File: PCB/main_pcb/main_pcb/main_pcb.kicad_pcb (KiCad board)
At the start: 2 copper layers, 235 x 235 mm, 49 parts, among them J1 Conn_01x20_Socket, J10 B6B-XH-A, J11 B8B-XH-A, J12 B6B-XH-A, J13 B8B-XH-A, J14 B8B-XH-A, J2 Conn_01x20_Socket, J3 B02P-VL, J4 B02P-VL, J5 B8B-XH-A, J6 B8B-XH-A, J7 B8B-XH-A, J8 B8B-XH-A, J9 B6B-XH-A, U1 MCP3208, U10 APDS-9006-020, U11 APDS-9006-020, U12 APDS-9006-020, U2 MCP3208, U3 APDS-9006-020, U4 APDS-9006-020, U5 APDS-9006-020, U6 APDS-9006-020, U7 APDS-9006-020, U8 APDS-9006-020, U9 APDS-9006-020

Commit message: Started layout of the main PCB. God help me for I have sinned :(
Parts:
- J1, J2: footprint Connector_PinSocket_1.00mm:PinSocket_1x20_P1.00mm_Vertical -> Connector_PinSocket_2.54mm:PinSocket_1x20_P2.54mm_Vertical
- J5, J6, J7, J8: footprint B8B_XH_A:JST_B8B-XH-A -> Connector_JST:JST_XH_B8B-XH-A_1x08_P2.50mm_Vertical
- moved J6 217.6 mm to (23.0, 24.5)
- moved U1 157.0 mm to (33.4, 83.4), turned to 180 degrees
- moved U2 131.1 mm to (168.8, 101.4)
- moved J3 125.8 mm to (148.5, 153.5)
- moved J11 106.2 mm to (46.5, 163.0)
- moved J12 104.2 mm to (80.0, 163.0)
- moved J14 98.3 mm to (173.0, 137.0)
- moved J4 97.6 mm to (173.1, 153.5)
- moved J13 82.6 mm to (108.5, 163.0)
- moved C6 64.9 mm to (136.5, 105.0), turned to 180 degrees
- moved C7 63.9 mm to (136.5, 90.0), turned to 180 degrees
- moved C8 63.6 mm to (136.5, 75.5), turned to 180 degrees
- moved C5 63.4 mm to (136.5, 120.0), turned to 180 degrees
- moved J8 63.3 mm to (28.0, 74.5), turned to 90 degrees
- moved C9 62.9 mm to (136.5, 60.0), turned to 180 degrees
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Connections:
- C2 pad 1: OpIn2 -> OpIn4
- C2 pad 2: OpOut2 -> OpOut4
- C3 pad 1: OpIn3 -> OpIn5
- C3 pad 2: OpOut3 -> OpOut5
- C4 pad 1: OpIn4 -> OpIn8
- C4 pad 2: OpOut4 -> OpOut8
- C5 pad 1: OpIn5 -> OpIn9
- C5 pad 2: OpOut5 -> OpOut9
- C6 pad 1: OpIn6 -> OpIn7
- C6 pad 2: OpOut6 -> OpOut7
- C7 pad 1: OpIn7 -> OpIn6
- C7 pad 2: OpOut7 -> OpOut6
- C8 pad 1: OpIn8 -> OpIn3
- C8 pad 2: OpOut8 -> OpOut3
- C9 pad 1: OpIn9 -> OpIn2
- C9 pad 2: OpOut9 -> OpOut2
- J1 pad 2: SPI1_CDn_SD -> unconnected-(J1-Pin_2-Pad2)
- J13 pad 4: SPI1_TX -> GND
- J13 pad 5: SPI1_RX -> SPI1_TX
- J13 pad 6: SPI1_CSn_SD -> SPI1_RX
- J13 pad 7: SPI1_CDn_SD -> SPI1_CSn_SD
- J13 pad 8: unconnected-(J13-Pad8) -> GND
- J3 pad 2: GND -> HEATER_ON
- OpAmp1 pad 1: OpOut0 -> OpOut3
- OpAmp1 pad 10: OpIn2 -> OpIn0
- OpAmp1 pad 12: OpIn3 -> OpIn1
- OpAmp1 pad 14: OpOut3 -> OpOut1
- OpAmp1 pad 3: OpIn0 -> OpIn3
- OpAmp1 pad 5: OpIn1 -> OpIn2
- OpAmp1 pad 7: OpOut1 -> OpOut2
- OpAmp1 pad 8: OpOut2 -> OpOut0
- OpAmp2 pad 10: OpIn6 -> OpIn7
- OpAmp2 pad 12: OpIn7 -> OpIn6
- OpAmp2 pad 14: OpOut7 -> OpOut6
- OpAmp2 pad 8: OpOut6 -> OpOut7
- OpAmp3 pad 12: unconnected-(OpAmp3-IN4+-Pad12) -> OpIn9
- OpAmp3 pad 14: unconnected-(OpAmp3-OUT4-Pad14) -> OpOut9
- OpAmp3 pad 5: OpIn9 -> unconnected-(OpAmp3-IN2+-Pad5)
- OpAmp3 pad 7: OpOut9 -> unconnected-(OpAmp3-OUT2-Pad7)
- R2 pad 1: OpIn2 -> OpIn4
- R2 pad 2: OpOut2 -> OpOut4
- R3 pad 1: OpIn3 -> OpIn5
- R3 pad 2: OpOut3 -> OpOut5
- R4 pad 1: OpIn4 -> OpIn8
- R4 pad 2: OpOut4 -> OpOut8
- R5 pad 1: OpIn5 -> OpIn9
- R5 pad 2: OpOut5 -> OpOut9
- R6 pad 1: OpIn6 -> OpIn7
- R6 pad 2: OpOut6 -> OpOut7
- R7 pad 1: OpIn7 -> OpIn6
- R7 pad 2: OpOut7 -> OpOut6
- R8 pad 1: OpIn8 -> OpIn3
- R8 pad 2: OpOut8 -> OpOut3
- R9 pad 1: OpIn9 -> OpIn2
- R9 pad 2: OpOut9 -> OpOut2
- U1 pad 1: OpOut5 -> unconnected-(U1-CH0-Pad1)
- U1 pad 2: OpOut6 -> unconnected-(U1-CH1-Pad2)
- U1 pad 3: OpOut7 -> unconnected-(U1-CH2-Pad3)
- U1 pad 5: OpOut9 -> OpOut5
- U1 pad 6: unconnected-(U1-CH5-Pad6) -> OpOut4
- U1 pad 7: unconnected-(U1-CH6-Pad7) -> OpOut1
- U1 pad 8: unconnected-(U1-CH7-Pad8) -> OpOut0
- U10 pad 1: OpIn7 -> OpIn6
- U11 pad 1: OpIn8 -> OpIn3
- U12 pad 1: OpIn9 -> OpIn2
- U2 pad 1: OpOut0 -> OpOut2
- U2 pad 2: OpOut1 -> OpOut3
- U2 pad 3: OpOut2 -> OpOut6
- U2 pad 4: OpOut3 -> OpOut7
- U2 pad 5: OpOut4 -> OpOut9
- U4 pad 1: OpIn1 -> unconnected-(U4-OUT-Pad1)
- U4 pad 2: +3.3V -> unconnected-(U4-VCC-Pad2)
- U4 pad 3: +3.3V -> unconnected-(U4-VCC__1-Pad3)
- U5 pad 1: OpIn2 -> OpIn4
- U6 pad 1: OpIn3 -> OpIn5
- U7 pad 1: OpIn4 -> OpIn8
- U8 pad 1: OpIn5 -> OpIn9
- U9 pad 1: OpIn6 -> OpIn7
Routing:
- net +3.3V: track 0.00 -> 298.7 mm
- net I2C0_SCL: track 0.00 -> 200.8 mm
- net I2C0_SDA: track 0.00 -> 191.3 mm
- net TEMP_ALERT: track 0.00 -> 183.7 mm
- net OpOut7: track 0.00 -> 92.4 mm
- net OpOut5: track 0.00 -> 91.6 mm
- net OpOut9: track 0.00 -> 84.3 mm
- net OpOut8: track 0.00 -> 83.0 mm
- net OpOut0: track 0.00 -> 82.4 mm
- net OpOut2: track 0.00 -> 81.2 mm
- net OpOut1: track 0.00 -> 74.8 mm
- net OpOut3: track 0.00 -> 74.6 mm
- net OpOut6: track 0.00 -> 63.5 mm
- net OpOut4: track 0.00 -> 63.4 mm
- net OpIn8: track 0.00 -> 60.6 mm
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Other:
- board size 235 x 235 mm -> 172 x 155 mm

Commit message: And falling into a place where two layers met, they ran the PCB  aground; and the forepart stuck fast, and remained unmoveable, but the hinder part was broken with the violence of the photodiodes.
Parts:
- moved J2 55.0 mm to (74.4, 153.5), turned to -90 degrees
- moved J1 46.1 mm to (74.4, 135.7), turned to -90 degrees
- moved J10 12.4 mm to (94.8, 52.6), turned to 0 degrees
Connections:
- J10 pad 3: SPI1_TX -> SPI1_RX
- J10 pad 4: SPI1_CSn_TD1 -> SPI1_SCK
- J10 pad 5: SPI1_SCK -> SPI1_TX
- J10 pad 6: SPI1_RX -> SPI1_CSn_TD1
- J13 pad 3: SPI1_SCK -> SPI1_TX
- J13 pad 5: SPI1_TX -> SPI1_SCK
- J2 pad 10: SPI1_CSn_TD1 -> SPI1_CSn_TD0
- J2 pad 9: SPI1_CSn_TD0 -> SPI1_CSn_TD1
- J9 pad 3: SPI1_TX -> SPI1_RX
- J9 pad 4: SPI1_CSn_TD0 -> SPI1_SCK
- J9 pad 5: SPI1_SCK -> SPI1_TX
- J9 pad 6: SPI1_RX -> SPI1_CSn_TD0
- U4 pad 1: unconnected-(U4-OUT-Pad1) -> OpIn1
- U4 pad 2: unconnected-(U4-VCC-Pad2) -> +3.3V
- U4 pad 3: unconnected-(U4-VCC__1-Pad3) -> +3.3V
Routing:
- net +3.3V: track 298.7 -> 985.8 mm, vias 0 -> 16
- net SPI1_TX: track 0.00 -> 390.7 mm
- net SPI1_SCK: track 0.00 -> 377.7 mm
- net SPI1_RX: track 0.00 -> 367.6 mm
- net +5V: track 44.4 -> 202.1 mm, vias 0 -> 4
- net SPI1_CSn_TD1: track 0.00 -> 147.5 mm
- net SPI1_CSn_ADC1: track 0.00 -> 138.6 mm
- net GND: track 0.00 -> 105.3 mm, vias 0 -> 12
- net HEATER_ON: track 0.00 -> 99.9 mm
- net TEMP_ALERT: track 183.7 -> 275.7 mm
- net I2C0_SDA: track 191.3 -> 278.6 mm
- net I2C0_SCL: track 200.8 -> 281.3 mm
- net BTN0: track 0.00 -> 69.8 mm
- net BTN1: track 0.00 -> 68.6 mm
- net SPI1_CSn_TD0: track 0.00 -> 65.2 mm
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- added copper zone on B.Cu, net GND
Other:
- outline, holes or cut-outs redrawn

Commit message: The PCB is the resurrection and the life; he that believeth in it, though it were dead, yet shall he live.
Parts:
- U10, U11, U12, U3, U4, U5, U6, U7, U8, U9: footprint APDS_9006_020:XDCR_APDS-9006-020 -> APDS_9006_020:photodiode_v3
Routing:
- net GND: track 105.3 -> 109.3 mm, vias 12 -> 14
- net +3.3V: track 985.8 -> 985.3 mm

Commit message: Rejoice always, pray continually, give thanks in all circumstances, for this is the PCB’s will for you.
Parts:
- renumbered U2 to ADC0, U1 to ADC1, J12 to BTN_Header1, J14 to Fan_Header1, J11 to LCD_Header1, U3 to Photo0, U4 to Photo1, U12 to Photo2, U11 to Photo3, U5 to Photo4, U6 to Photo5, U9 to Photo7, U7 to Photo8, U8 to Photo9, J3 to Power_Connector_3V3, J4 to Power_Connector_5V, J13 to SD_Header1, J9 to SW0_Header1, J10 to SW1_Header1, J8 to Temp0_Header, J7 to Temp1_Header, J6 to Temp2_Header, J5 to Temp3_Header, U10 to UPhoto6
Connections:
- Temp1_Header pad 6: unconnected-(J7-Pad6) -> +3.3V
- Temp2_Header pad 7: unconnected-(J6-Pad7) -> +3.3V
- Temp3_Header pad 6: unconnected-(J5-Pad6) -> +3.3V
- Temp3_Header pad 7: unconnected-(J5-Pad7) -> +3.3V
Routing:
- net +3.3V: track 985.3 -> 1032.0 mm, vias 16 -> 17
- net GND: track 109.3 -> 130.6 mm
- net TEMP_ALERT: track 275.7 -> 273.4 mm
- net I2C0_SDA: track 278.6 -> 276.4 mm
- net I2C0_SCL: track 281.3 -> 280.5 mm

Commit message: When a man's ways please the PCB, he makes even his enemies to be at peace with him
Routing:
- net BTN1: track 68.6 -> 69.8 mm
- net BTN0: track 69.8 -> 71.0 mm
- net BTN2: track 65.0 -> 66.1 mm
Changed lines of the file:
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@@
+	)
+	(segment
+		(start 82.5 157.2013)
+		(end 70.2987 145)
+		(width 0.2)
+		(layer "F.Cu")
+		(net 22)
+	)
+	(segment
+		(start 70.2987 145)
+		(end 35.46 145)
+		(width 0.2)
+		(layer "F.Cu")
+		(net 22)
 	)
 	(segment
 		(start 82.5 163)
-		(end 82.5 159.258)
-		(width 0.2)
-		(layer "F.Cu")
-		(net 22)
-	)
-	(segment
-		(start 68.242 145)
-		(end 35.46 145)
-		(width 0.2)
-		(layer "F.Cu")
-		(net 22)
-	)
-	(segment
-		(start 82.5 159.258)
-		(end 68.242 145)
+		(end 82.5 157.2013)
 		(width 0.2)
 		(layer "F.Cu")
@@
 	)
 	(segment
-		(start 85 161.1909)
-		(end 68.3091 144.5)
+		(start 70.3658 144.5)
+		(end 37.5 144.5)
 		(width 0.2)
 		(layer "F.Cu")
@@
 	)
 	(segment
-		(start 68.3091 144.5)
-		(end 37.5 144.5)
+		(start 85 163)
+		(end 85 159.1342)
+		(width 0.2)
+		(layer "F.Cu")
+		(net 27)
+	)
+	(segment
+		(start 85 159.1342)
+		(end 70.3658 144.5)
 		(width 0.2)
 		(layer "F.Cu")
@@
 	)
 	(segment
-		(start 85 163)
-		(end 85 161.1909)
-		(width 0.2)
-		(layer "F.Cu")
-		(net 27)
-	)
-	(segment
 		(start 42.08 144)
 		(end 33.8 135.72)
@@
 	)
 	(segment
-		(start 68.5 144)
+		(start 87.5 161.0671)
+		(end 70.4329 144)
+		(width 0.2)
+		(layer "F.Cu")
+		(net 28)
+	)
+	(segment
+		(start 70.4329 144)
 		(end 42.08 144)
 		(width 0.2)
@@
 	(segment
 		(start 87.5 163)
-		(end 68.5 144)
-		(width 0.2)
-		(layer "F.Cu")
+		(end 87.5 161.0671)
+		(width 0.2)
+		(layer "F.Cu")

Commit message: Do not fear, for the PCB hath redeemed you. It has called you by name, and you belong to it
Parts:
- moved Temp2_Header 12.5 mm to (23.0, 37.0)
- moved Temp3_Header 11.0 mm to (175.5, 37.0)
- moved Temp1_Header 10.0 mm to (23.0, 47.0)
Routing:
- net +3.3V: track 1032.0 -> 1016.5 mm
- net I2C0_SDA: track 276.4 -> 261.8 mm
- net I2C0_SCL: track 280.5 -> 266.1 mm
- net TEMP_ALERT: track 273.4 -> 259.6 mm
- net GND: track 130.6 -> 140.6 mm
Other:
- board size 172 x 155 mm -> 163.5 x 142.5 mm

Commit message: There is none holy like the PCB: for there is none besides it; there is no rock like our PCB
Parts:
- moved Temp3_Header 6.00 mm to (169.5, 37.0)
- moved Temp2_Header 1.50 mm to (23.0, 38.5)
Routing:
- net +3.3V: track 1016.5 -> 1009.7 mm
- net TEMP_ALERT: track 259.6 -> 253.6 mm
- net I2C0_SCL: track 266.1 -> 260.1 mm
- net I2C0_SDA: track 261.8 -> 255.8 mm
- net GND: track 140.6 -> 139.1 mm
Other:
- outline, holes or cut-outs redrawn

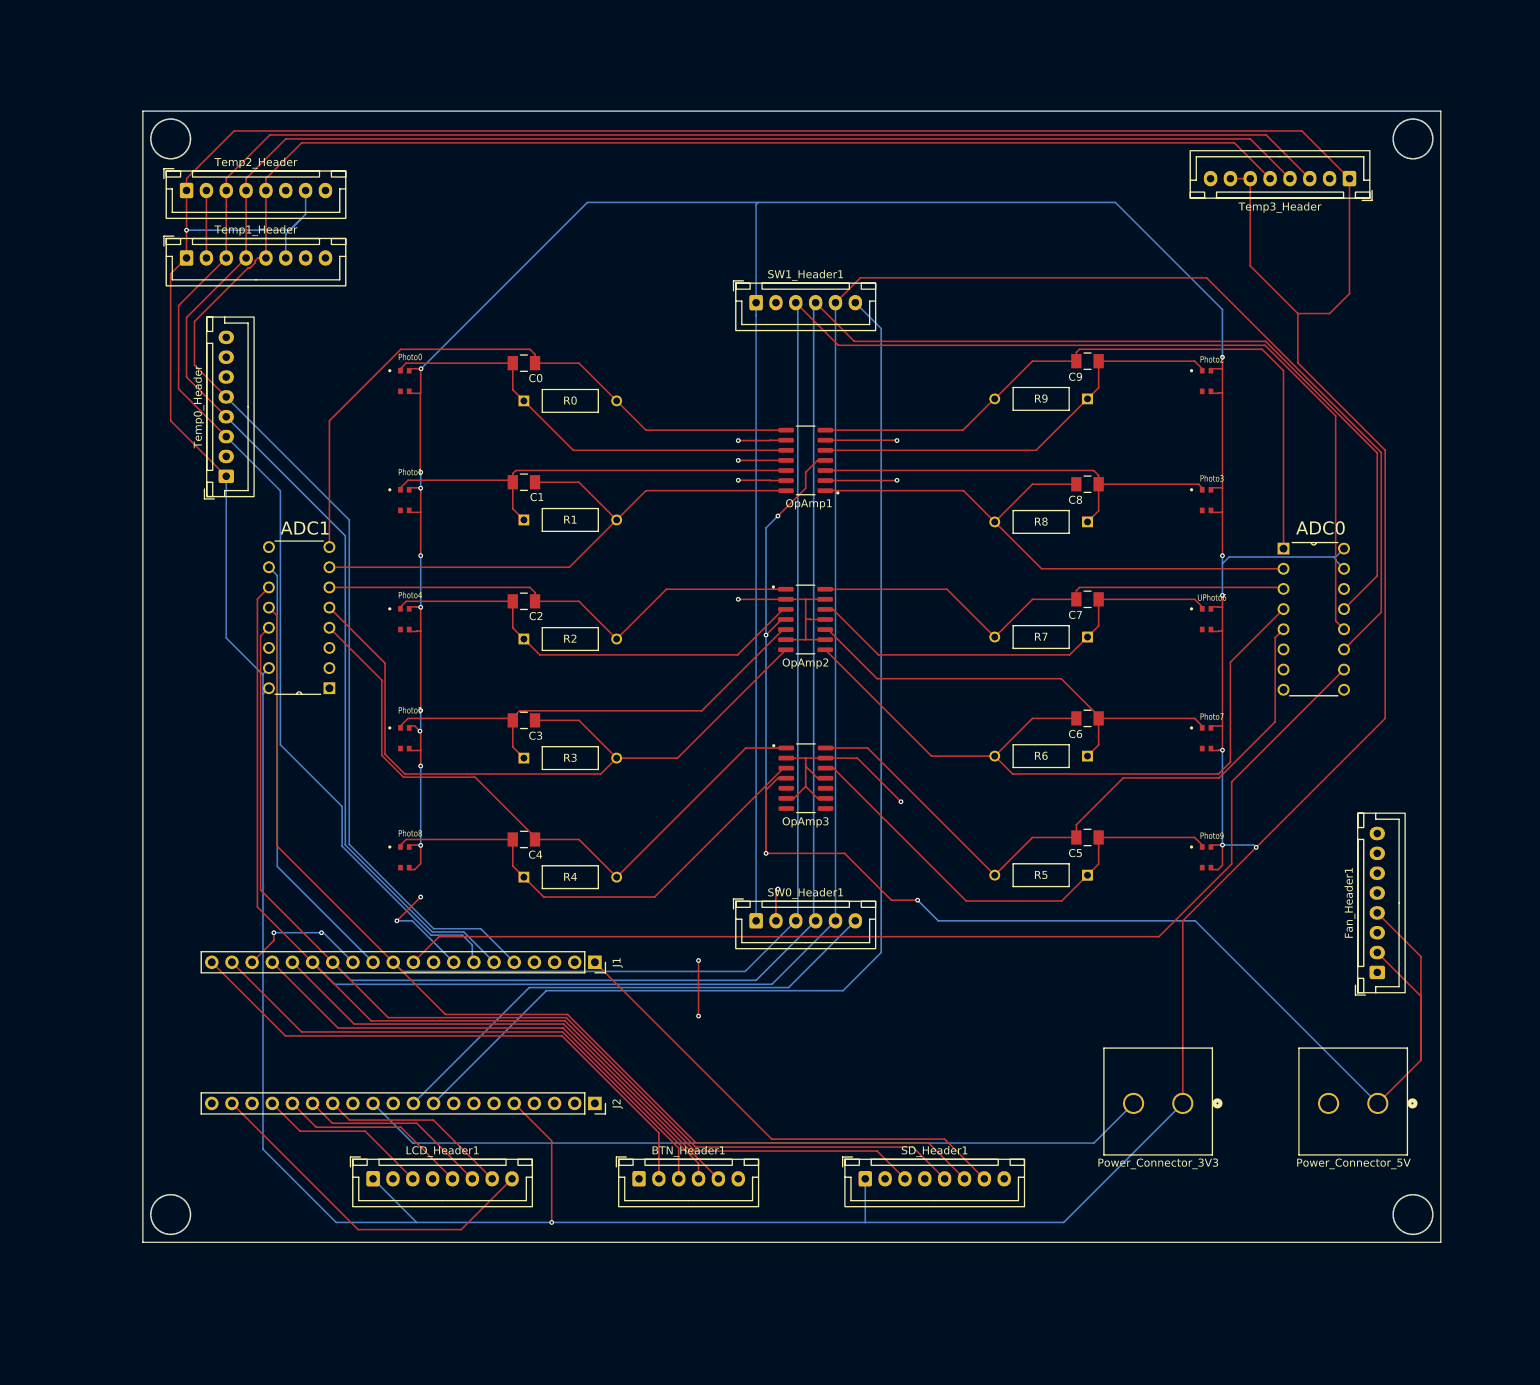
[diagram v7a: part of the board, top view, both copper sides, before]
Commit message: Added ground plane to top layer of PCB.
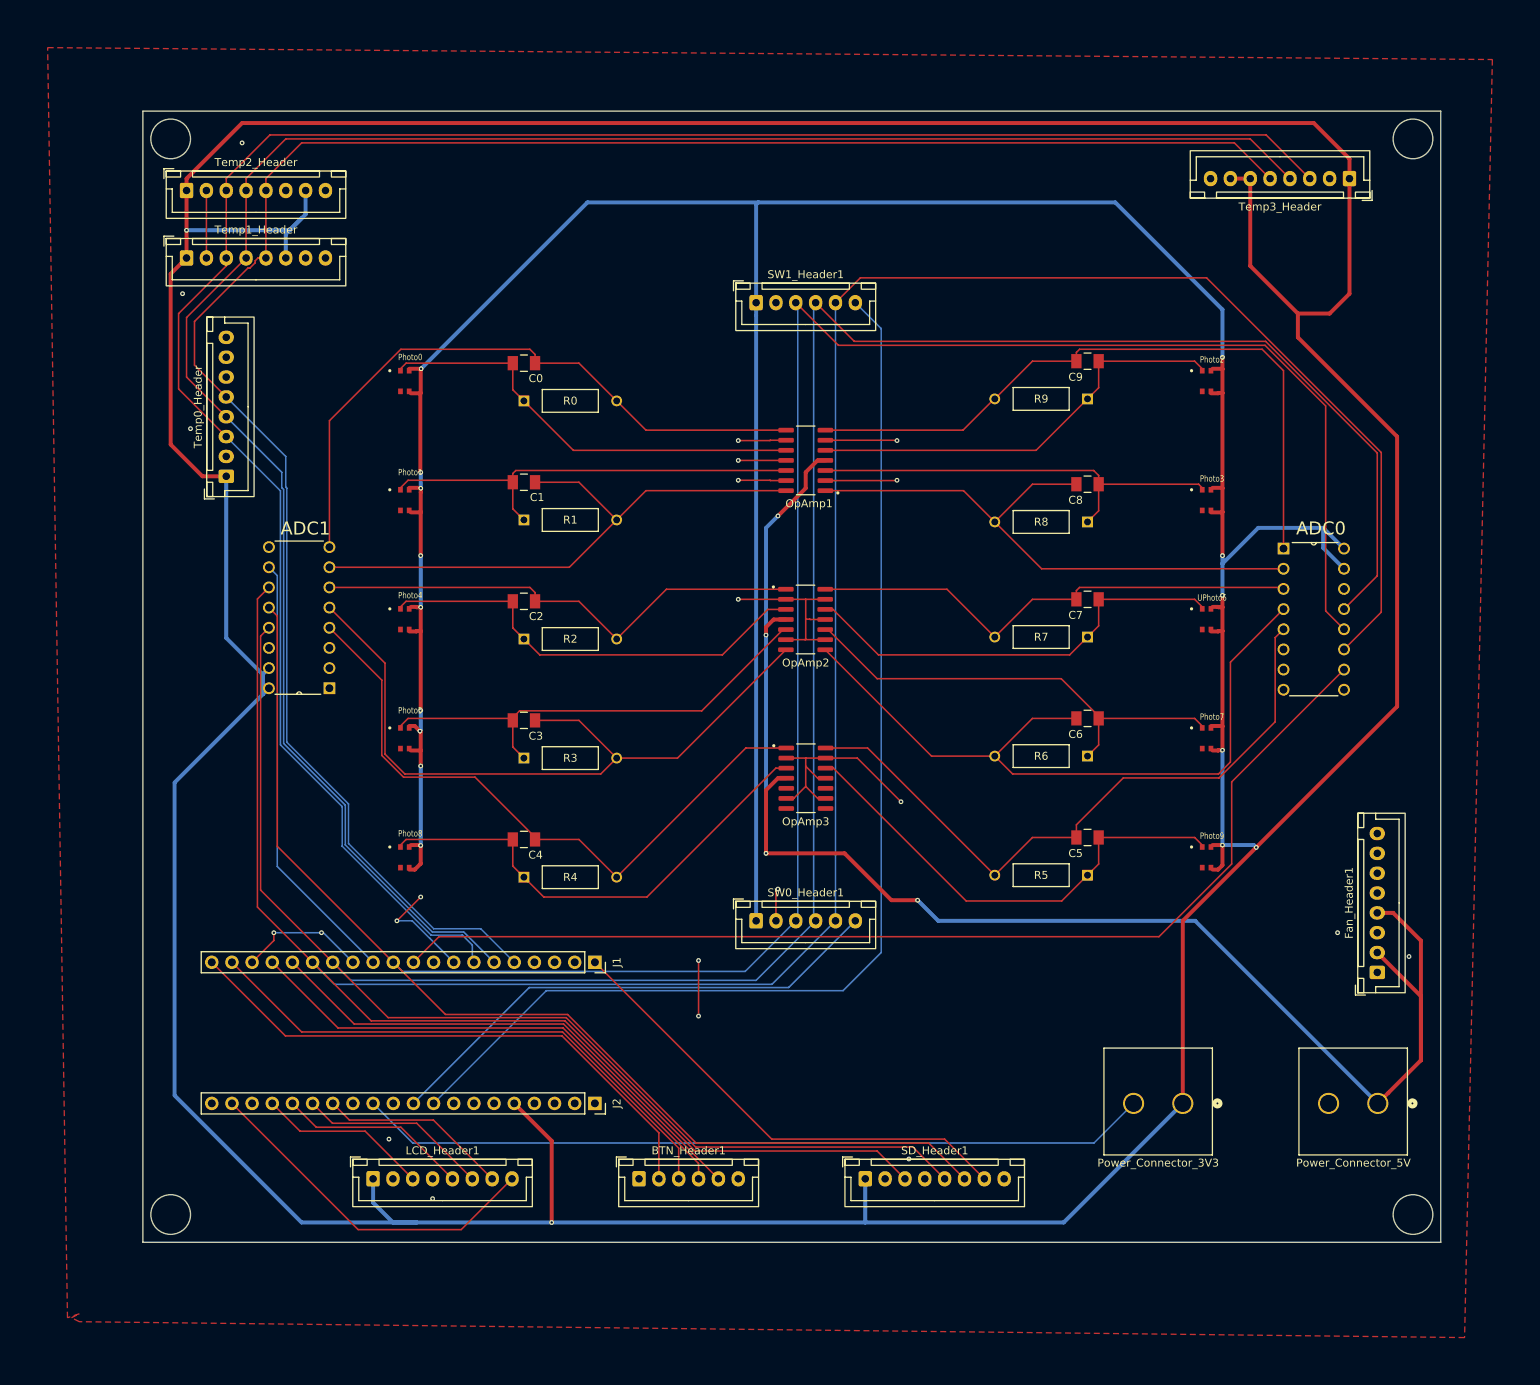
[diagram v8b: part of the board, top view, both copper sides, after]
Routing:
- net +3.3V: track 1009.7 -> 1034.8 mm
- net +5V: track 202.1 -> 203.9 mm
- net GND: vias 14 -> 22
- added copper zone on F.Cu, net GND
